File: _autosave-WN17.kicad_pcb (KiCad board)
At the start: 2 copper layers, 41 x 46 mm, 14 parts, among them J1 Conn_01x02_Pin, U1 AS5600, U2 DRV8434APWPR, U3 STM32L476RGTx, U4 ESP-12F, U5 AMS1117

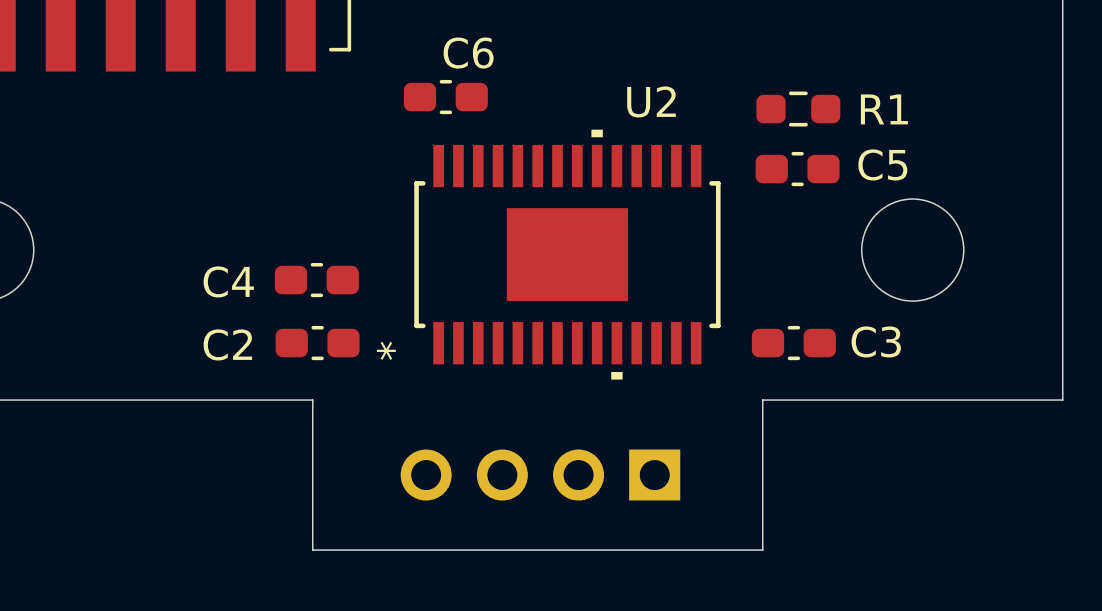
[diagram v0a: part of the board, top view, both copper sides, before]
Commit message: Etiquetas y pines modulo driver
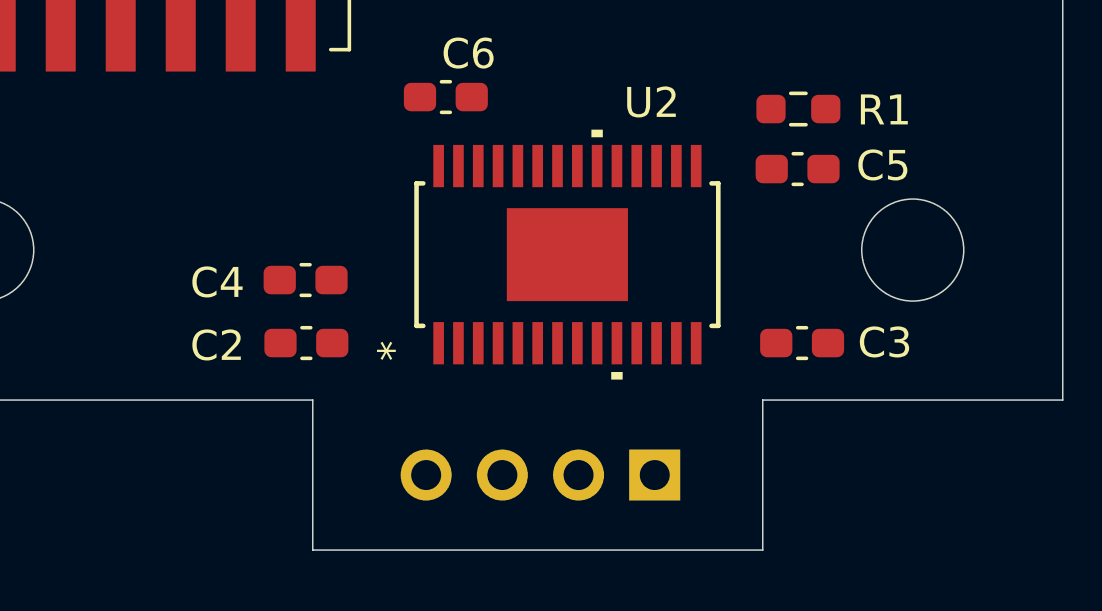
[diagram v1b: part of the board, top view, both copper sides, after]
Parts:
- moved C2 0.38 mm to (110.8, 94.1)
- moved C4 0.38 mm to (110.8, 92.0)
- moved C3 0.28 mm to (127.3, 94.1)
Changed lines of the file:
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@@
 	(footprint "Capacitor_SMD:C_0603_1608Metric_Pad1.08x0.95mm_HandSolder"
 		(layer "F.Cu")
-		(at 111.1375 92)
+		(at 110.7625 92)
 		(descr "Capacitor SMD 0603 (1608 Metric), square (rectangular) end terminal, IPC_7351 nominal with elongated pad for handsoldering. (Body size source: IPC-SM-782 page 76, https://www.pcb-3d.com/wordpress/wp-content/uploads/ipc-sm-782a_amendment_1_and_2.pdf), generated with kicad-footprint-generator")
 		(tags "capacitor handsolder")
@@
 	(footprint "Capacitor_SMD:C_0603_1608Metric_Pad1.08x0.95mm_HandSolder"
 		(layer "F.Cu")
-		(at 127.0375 94.1)
+		(at 127.3125 94.1)
 		(descr "Capacitor SMD 0603 (1608 Metric), square (rectangular) end terminal, IPC_7351 nominal with elongated pad for handsoldering. (Body size source: IPC-SM-782 page 76, https://www.pcb-3d.com/wordpress/wp-content/uploads/ipc-sm-782a_amendment_1_and_2.pdf), generated with kicad-footprint-generator")
 		(tags "capacitor handsolder")
@@
 	(footprint "Capacitor_SMD:C_0603_1608Metric_Pad1.08x0.95mm_HandSolder"
 		(layer "F.Cu")
-		(at 111.1625 94.1 180)
+		(at 110.7875 94.1 180)
 		(descr "Capacitor SMD 0603 (1608 Metric), square (rectangular) end terminal, IPC_7351 nominal with elongated pad for handsoldering. (Body size source: IPC-SM-782 page 76, https://www.pcb-3d.com/wordpress/wp-content/uploads/ipc-sm-782a_amendment_1_and_2.pdf), generated with kicad-footprint-generator")
 		(tags "capacitor handsolder")
